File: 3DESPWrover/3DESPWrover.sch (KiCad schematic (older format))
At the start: 23 parts, among them J1 Conn_01x05_Male, J2 Conn_01x03_Female, J3 Conn_02x03_Odd_Even, J4 Conn_02x07_Odd_Even, SW1 SW_Push, SW2 SW_Push, U1 ESP32-S2-WROVER

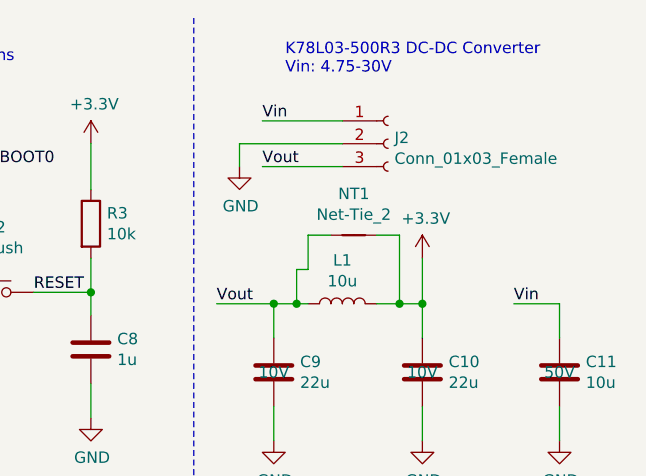
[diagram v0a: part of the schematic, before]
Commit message: Replaced TE connector and regulator to smd on top board
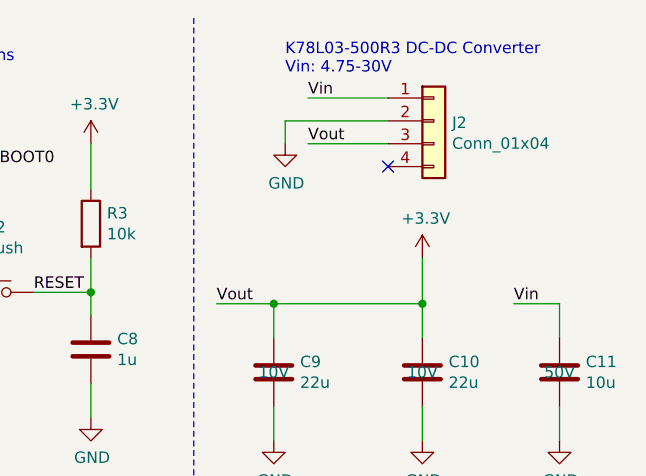
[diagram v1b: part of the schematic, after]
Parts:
- removed J2: Conn_01x03_Female, Connector_PinHeader_2.54mm:PinHeader_1x03_P2.54mm_Vertical, symbol Connector:Conn_01x03_Female
- removed L1: 10u, Custom:L_4.5x4_H3.2, symbol Device:L
- removed NT1: Net-Tie_2, NetTie:NetTie-2_SMD_Pad0.5mm, symbol Device:Net-Tie_2
- added J2: Conn_01x04, Custom:K7803JT-500R3-SMD, symbol Connector_Generic:Conn_01x04
- J4: footprint Custom:TE_Micromatch_2,54_14 -> Custom:TE_Micromatch_2,54_14_SMD
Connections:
- net Vout is gone; now on net +3V3: C9.1
- net +3V3: now also J2.3 (Pin_3)
- net GND: now also J2.2 (Pin_2)
- net Vin: now also J2.1 (Pin_1)
- no-connect marks 1 -> 2
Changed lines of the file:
@@
 Wire Wire Line
 	3600 3500 3600 3300
-$Comp
-L Connector:Conn_01x03_Female J2
-U 1 1 61BC5370
-P 10200 1000
-F 0 "J2" H 10228 1026 50  0000 L CNN
-F 1 "Conn_01x03_Female" H 10228 935 50  0000 L CNN
-F 2 "Connector_PinHeader_2.54mm:PinHeader_1x03_P2.54mm_Vertical" H 10200 1000 50  0001 C CNN
-F 3 "~" H 10200 1000 50  0001 C CNN
-	1    10200 1000
-	1    0    0    -1
-$EndComp
-Wire Wire Line
-	10000 900  9650 900
-Text Label 9650 900  0    50   ~ 0
+Wire Wire Line
+	10200 800  9850 800
+Text Label 9850 800  0    50   ~ 0
 Vin
 Wire Wire Line
-	10000 1100 9650 1100
-Text Label 9650 1100 0    50   ~ 0
+	10200 1000 9850 1000
+Text Label 9850 1000 0    50   ~ 0
 Vout
 $Comp
 L power:GND #PWR023
 U 1 1 61BD0ED8
-P 9550 1100
-F 0 "#PWR023" H 9550 850 50  0001 C CNN
-F 1 "GND" H 9555 927 50  0000 C CNN
-F 2 "" H 9550 1100 50  0001 C CNN
-F 3 "" H 9550 1100 50  0001 C CNN
-	1    9550 1100
-	1    0    0    -1
-$EndComp
-Wire Wire Line
-	10000 1000 9550 1000
-Wire Wire Line
-	9550 1000 9550 1100
+P 9750 1000
+F 0 "#PWR023" H 9750 750 50  0001 C CNN
+F 1 "GND" H 9755 827 50  0000 C CNN
+F 2 "" H 9750 1000 50  0001 C CNN
+F 3 "" H 9750 1000 50  0001 C CNN
+	1    9750 1000
+	1    0    0    -1
+$EndComp
+Wire Wire Line
+	10200 900  9750 900
+Wire Wire Line
+	9750 900  9750 1000
 $Comp
 L Device:C C9
@@
 Wire Wire Line
 	10350 2150 10350 2300
-$Comp
-L Device:L L1
-U 1 1 61BDD5BF
-P 10000 1700
-F 0 "L1" V 10190 1700 50  0000 C CNN
-F 1 "10u" V 10099 1700 50  0000 C CNN
-F 2 "Custom:L_4.5x4_H3.2" H 10000 1700 50  0001 C CNN
-F 3 "~" H 10000 1700 50  0001 C CNN
-	1    10000 1700
-	0    -1   -1   0
-$EndComp
-Wire Wire Line
-	9700 1700 9800 1700
 Connection ~ 9700 1700
-Wire Wire Line
-	10150 1700 10250 1700
 Text Label 9450 1700 0    50   ~ 0
 Vout
@@
 F 0 "J4" H 7850 4067 50  0000 C CNN
 F 1 "Conn_02x07_Odd_Even" H 7850 3976 50  0000 C CNN
-F 2 "Custom:TE_Micromatch_2,54_14" H 7800 3550 50  0001 C CNN
+F 2 "Custom:TE_Micromatch_2,54_14_SMD" H 7800 3550 50  0001 C CNN
 F 3 "~" H 7800 3550 50  0001 C CNN
 	1    7800 3550
@@
 Wire Wire Line
 	750  3900 750  3800
-$Comp
-L Device:Net-Tie_2 NT1
-U 1 1 61C3CDD7
-P 10050 1400
-F 0 "NT1" H 10050 1581 50  0000 C CNN
-F 1 "Net-Tie_2" H 10050 1490 50  0000 C CNN
-F 2 "NetTie:NetTie-2_SMD_Pad0.5mm" H 10050 1400 50  0001 C CNN
-F 3 "~" H 10050 1400 50  0001 C CNN
-	1    10050 1400
-	1    0    0    -1
-$EndComp
-Wire Wire Line
-	9950 1400 9850 1400
-Wire Wire Line
-	9850 1400 9850 1550
-Wire Wire Line
-	9850 1550 9800 1550
-Wire Wire Line
-	9800 1550 9800 1700
-Connection ~ 9800 1700
-Wire Wire Line
-	9800 1700 9850 1700
-Wire Wire Line
-	10150 1400 10250 1400
-Wire Wire Line
-	10250 1400 10250 1700
-Connection ~ 10250 1700
-Wire Wire Line
-	10250 1700 10350 1700
 Wire Wire Line
 	5850 3650 5600 3650
@@
 	6750 3650 6600 3650
 Connection ~ 6600 3650
+$Comp
+L Connector_Generic:Conn_01x04 J2
+U 1 1 628687F4
+P 10400 900
+F 0 "J2" H 10480 892 50  0000 L CNN
+F 1 "Conn_01x04" H 10480 801 50  0000 L CNN
+F 2 "Custom:K7803JT-500R3-SMD" H 10400 900 50  0001 C CNN
+F 3 "~" H 10400 900 50  0001 C CNN
+	1    10400 900
+	1    0    0    -1
+$EndComp
+NoConn ~ 10200 1100
+Wire Wire Line
+	9700 1700 10350 1700
 $EndSCHEMATC
